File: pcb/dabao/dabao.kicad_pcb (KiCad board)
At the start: 2 copper layers, 127.8 x 107.8 mm, 68 parts, among them J1 Conn_01x05, J2 USB_C_Receptacle_USB2.0_16P, J3 Conn_01x04, J4 Conn_01x04_Pin, J5 Conn_Battery, J6 Conn_01x04, J7 Conn_01x04, J8 Display, SW1 SW_RESET, SW2 SW_POWER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

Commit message: Update layout
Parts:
- removed R4, R5: 4.7k, Resistor_SMD:R_0805_2012Metric
- J5: footprint Connector_JST:JST_EH_S2B-EH_1x02_P2.50mm_Horizontal -> Connector_JST:JST_PH_S2B-PH-K_1x02_P2.00mm_Horizontal
- JP6, R1: moved to F.Cu
- JP7: moved to B.Cu
- moved SW1 81.2 mm to (193.8, 109.8), turned to 90 degrees
- moved J6 42.7 mm to (152.8, 111.0), turned to 165 degrees
- moved J7 42.7 mm to (152.5, 112.2), turned to -15 degrees
- moved R3 28.6 mm to (209.8, 114.5), turned to -90 degrees
- moved J5 26.2 mm to (209.5, 136.5)
- moved R2 24.5 mm to (207.0, 114.5), turned to -90 degrees
- moved R1 22.9 mm to (204.2, 114.5), turned to -90 degrees
- moved JP9 17.5 mm to (202.0, 124.8), turned to -90 degrees
- moved JP10 15.1 mm to (204.8, 124.8), turned to -90 degrees
- moved JP12 12.4 mm to (211.2, 124.8), turned to -90 degrees
- moved JP11 12.4 mm to (208.5, 124.8), turned to -90 degrees
- moved JP1 12.1 mm to (214.0, 145.2)
- moved JP3 12.0 mm to (214.0, 145.2)
- moved JP2 11.9 mm to (214.0, 148.0)
- moved JP4 11.8 mm to (214.0, 148.0)
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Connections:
- J1 pad 1: /SDA_Right -> /PS2_Data
- J1 pad 3: /SCL_Right -> /PS2_CLK
- J4 pad 1: unconnected-(J4-Pin_1-Pad1) -> VDD
- J4 pad 4: unconnected-(J4-Pin_4-Pad4) -> GND
- J5 pad 1: Net-(J5-Pin_1) -> GND
- J5 pad 2: GND -> Net-(J5-Pin_2)
- SW2 pad 2: Net-(J5-Pin_1) -> Net-(J5-Pin_2)
- U1 pad 1: /SDA_Right -> unconnected-(U1-P0.06-Pad1)
- U1 pad 10: /col_index -> /SCL_Right
- U1 pad 11: /col_middle -> /SDA_Right
- U1 pad 12: /col_ring -> /row_thumb
- U1 pad 17: /MOSI -> /row_top
- U1 pad 18: /SCK -> /row_home
- U1 pad 19: /CS -> /row_bottom
- U1 pad 2: /SCL_Right -> unconnected-(U1-P0.08-Pad2)
- U1 pad 20: unconnected-(U1-P1.15-LF-Pad20) -> /col_inner
- U1 pad 21: unconnected-(U1-P1.13-LF-Pad21) -> /col_index
- U1 pad 22: unconnected-(U1-P1.11-LF-Pad22) -> /col_middle
- U1 pad 23: unconnected-(U1-P0.10-LF-Pad23) -> /col_ring
- U1 pad 5: /row_top -> /PS2_Data
- U1 pad 6: /row_home -> /PS2_CLK
- U1 pad 7: /row_bottom -> /MOSI
- U1 pad 8: /row_thumb -> /SCK
- U1 pad 9: /col_inner -> /CS
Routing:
- net /SDA_Right: track 66.4 -> 33.1 mm, vias 0 -> 2
- net /MOSI: track 0.00 -> 18.9 mm
- net /SCL_Right: track 16.8 -> 34.9 mm
- net /SCK: track 0.00 -> 16.4 mm
- net Net-(J4-Pin_3): track 6.71 -> 22.3 mm
- net Net-(J4-Pin_2): track 6.48 -> 21.5 mm
- net /CS: track 0.00 -> 13.0 mm
- net Net-(J8-Pin_1): track 0.00 -> 11.6 mm, vias 0 -> 2
- net Net-(J8-Pin_2): track 0.00 -> 11.6 mm, vias 0 -> 2
- net /SDA_Left: track 0.00 -> 7.01 mm, vias 0 -> 2
- net Net-(JP1-B): track 8.06 -> 14.4 mm
- net Net-(JP2-B): track 9.56 -> 10.2 mm, vias 1 -> 0
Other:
- board text added: "+"
- board text added: "I2C"
- board text added: "LEFT"
- board text added: "RIGHT"
- board text added: "SPI"

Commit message: Clean up schematic
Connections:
- net Net-(U1-RST) renamed /RESET
- R2 pad 2: /SCL_Left -> /SCL_Right
- R3 pad 2: /SDA_Left -> /SDA_Right
- SW2 pad 1: Net-(SW2-A) -> /BAT+
- U1 pad 1: unconnected-(U1-P0.06-Pad1) -> /PS2_Data
- U1 pad 10: /SCL_Right -> /CS
- U1 pad 11: /SDA_Right -> unconnected-(U1-P1.04-LF-Pad11)
- U1 pad 13: unconnected-(U1-BAT+-Pad13) -> /BAT+
- U1 pad 2: unconnected-(U1-P0.08-Pad2) -> /PS2_CLK
- U1 pad 29: Net-(SW2-A) -> unconnected-(U1-BAT+-Pad29)
- U1 pad 3: unconnected-(U1-GND-Pad3) -> GND
- U1 pad 4: unconnected-(U1-GND-Pad4) -> GND
- U1 pad 5: /PS2_Data -> /SDA_Right
- U1 pad 6: /PS2_CLK -> /SCL_Right
- U1 pad 7: /MOSI -> /SCK
- U1 pad 8: /SCK -> unconnected-(U1-P0.24-Pad8)
- U1 pad 9: /CS -> /MOSI
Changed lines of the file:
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@@
 	(net 43 "Net-(J3-Pin_2)")
 	(net 44 "unconnected-(U1-P1.02-LF-Pad26)")
-	(net 45 "unconnected-(U1-BAT+-Pad13)")
+	(net 45 "/RESET")
 	(net 46 "unconnected-(U1-P1.01-LF-Pad25)")
 	(net 47 "Net-(J3-Pin_3)")
-	(net 48 "unconnected-(U1-GND-Pad4)")
+	(net 48 "/BAT+")
 	(net 49 "unconnected-(U1-P1.07-LF-Pad27)")
-	(net 50 "unconnected-(U1-GND-Pad3)")
+	(net 50 "unconnected-(U1-P1.04-LF-Pad11)")
 	(net 51 "unconnected-(U2-NC-Pad14)")
 	(net 52 "Net-(J3-Pin_1)")
@@
 	(net 73 "Net-(J5-Pin_2)")
 	(net 74 "GND")
-	(net 75 "Net-(U1-RST)")
-	(net 76 "Net-(SW2-A)")
-	(net 77 "unconnected-(U1-P0.08-Pad2)")
-	(net 78 "unconnected-(U1-P0.06-Pad1)")
-	(net 79 "/PS2_Data")
-	(net 80 "/PS2_CLK")
+	(net 75 "unconnected-(U1-P0.24-Pad8)")
+	(net 76 "unconnected-(U1-BAT+-Pad29)")
+	(net 77 "/PS2_Data")
+	(net 78 "/PS2_CLK")
 	(footprint "Jumper:SolderJumper-2_P1.3mm_Open_TrianglePad1.0x1.5mm"
 		(layer "F.Cu")
@@
 			(layers "F.Cu" "F.Mask" "F.Paste")
 			(roundrect_rratio 0.243902)
-			(net 26 "/SDA_Left")
+			(net 30 "/SDA_Right")
 			(pintype "passive")
 		)
@@
 			(layers "F.Cu" "F.Mask" "F.Paste")
 			(roundrect_rratio 0.25)
-			(net 75 "Net-(U1-RST)")
+			(net 45 "/RESET")
 			(pinfunction "1")
 			(pintype "passive")
@@
 			(layers "F.Cu" "F.Mask" "F.Paste")
 			(roundrect_rratio 0.243902)
-			(net 25 "/SCL_Left")
+			(net 29 "/SCL_Right")
 			(pintype "passive")
 		)
@@
 		)
 		(fp_line
-			(start -1.5 -2.899999)
+			(start -1.5 -2.899998)
 			(end -1.5 -1.4)
 			(stroke
@@
 		(fp_line
 			(start -0.1 -2.9)
-			(end -1.5 -2.899999)
+			(end -1.5 -2.899998)
 			(stroke
 				(width 0.08)
@@
 		(fp_line
 			(start -1.5 -1.4)
-			(end -1.5 -2.899999)
+			(end -1.5 -2.899998)
 			(stroke
 				(width 0.05)
@@
 		)
 		(fp_line
-			(start -1.5 -2.899999)
+			(start -1.5 -2.899998)
 			(end 1.5 -2.9)
 			(stroke
@@
 		)
 		(fp_line
-			(start -1.5 -2.899999)
+			(start -1.5 -2.899998)
 			(end -1.5 -1.4)
 			(stroke
@@
 		(fp_line
 			(start -0.1 -2.9)
-			(end -1.5 -2.899999)
+			(end -1.5 -2.899998)
 			(stroke
 				(width 0.08)
@@
 			(layers "F.Cu" "F.Mask" "F.Paste")
 			(roundrect_rratio 0.15)
-			(net 76 "Net-(SW2-A)")
+			(net 48 "/BAT+")
 			(pinfunction "A")
 			(pintype "passive")
@@
 		)
 		(fp_line
-			(start 7 4.999999)
+			(start 7 4.999998)
 			(end 9.5 5)
 			(stroke
@@
 		)
 		(fp_line
-			(start 7 4.999999)
+			(start 7 4.999998)
 			(end 9.5 5)
 			(stroke
@@
 		)
 		(fp_line
-			(start 7 4.999999)
+			(start 7 4.999998)
 			(end 9.5 5)
 			(stroke
@@
 		)
 		(fp_line
-			(start 7 4.999999)
+			(start 7 4.999998)
 			(end 9.5 5)
 			(stroke
@@
 		)
 		(fp_line
-			(start 7 4.999999)
+			(start 7 4.999998)
 			(end 9.5 5)
 			(stroke
@@
 		)
 		(fp_line
-			(start 7 4.999999)
+			(start 7 4.999998)
 			(end 9.5 5)
 			(stroke
@@
 		)
 		(fp_line
-			(start 7 4.999999)
+			(start 7 4.999998)
 			(end 9.5 5)
 			(stroke
@@
 		)
 		(fp_line
-			(start 7 4.999999)
+			(start 7 4.999998)
 			(end 9.5 5)
 			(stroke
@@
 			(layers "*.Cu" "F.Mask")
 			(remove_unused_layers no)
-			(net 78 "unconnected-(U1-P0.06-Pad1)")
+			(net 77 "/PS2_Data")
 			(pinfunction "P0.06")
 			(pintype "bidirectional")
@@
 			(layers "*.Cu" "F.Mask")
 			(remove_unused_layers no)
-			(net 77 "unconnected-(U1-P0.08-Pad2)")
+			(net 78 "/PS2_CLK")
 			(pinfunction "P0.08")
 			(pintype "bidirectional")
@@
 			(remove_unused_layers no)
 			(roundrect_rratio 0.25)
-			(net 50 "unconnected-(U1-GND-Pad3)")
+			(net 74 "GND")
 			(pinfunction "GND")
 			(pintype "power_out")
@@
 			(remove_unused_layers no)
 			(roundrect_rratio 0.25)
-			(net 48 "unconnected-(U1-GND-Pad4)")
+			(net 74 "GND")
 			(pinfunction "GND")
 			(pintype "power_out")
@@
 			(layers "*.Cu" "F.Mask")
 			(remove_unused_layers no)
-			(net 79 "/PS2_Data")
+			(net 30 "/SDA_Right")
 			(pinfunction "P0.17")
 			(pintype "bidirectional")
@@
 			(layers "*.Cu" "F.Mask")
 			(remove_unused_layers no)
-			(net 80 "/PS2_CLK")
+			(net 29 "/SCL_Right")
 			(pinfunction "P0.20")
 			(pintype "bidirectional")
@@
 			(layers "*.Cu" "F.Mask")
 			(remove_unused_layers no)
-			(net 71 "/MOSI")
+			(net 72 "/SCK")
 			(pinfunction "P0.22")
 			(pintype "bidirectional")
@@
 			(layers "*.Cu" "F.Mask")
 			(remove_unused_layers no)
-			(net 72 "/SCK")
+			(net 75 "unconnected-(U1-P0.24-Pad8)")
 			(pinfunction "P0.24")
 			(pintype "bidirectional")
@@
 			(layers "*.Cu" "F.Mask")
 			(remove_unused_layers no)
-			(net 70 "/CS")
+			(net 71 "/MOSI")
 			(pinfunction "P1.00")
 			(pintype "bidirectional")
@@
 			(layers "*.Cu" "F.Mask")
 			(remove_unused_layers no)
-			(net 29 "/SCL_Right")
+			(net 70 "/CS")
 			(pinfunction "P0.11")
 			(pintype "bidirectional")
@@
 			(layers "*.Cu" "F.Mask")
 			(remove_unused_layers no)
-			(net 30 "/SDA_Right")
+			(net 50 "unconnected-(U1-P1.04-LF-Pad11)")
 			(pinfunction "P1.04-LF")
 			(pintype "bidirectional")
@@
 			(layers "*.Cu" "F.Mask")
 			(remove_unused_layers no)
-			(net 45 "unconnected-(U1-BAT+-Pad13)")
+			(net 48 "/BAT+")
 			(pinfunction "BAT+")
 			(pintype "power_out")
@@
 			(layers "*.Cu" "F.Mask")
 			(remove_unused_layers no)
-			(net 75 "Net-(U1-RST)")
+			(net 45 "/RESET")
 			(pinfunction "RST")
 			(pintype "bidirectional")
@@
 			(layers "*.Cu" "F.Mask")
 			(remove_unused_layers no)
-			(net 76 "Net-(SW2-A)")
+			(net 76 "unconnected-(U1-BAT+-Pad29)")
 			(pinfunction "BAT+")
 			(pintype "power_out")
@@
 		)
 		(fp_line
-			(start 7 4.999999)
+			(start 7 4.999998)
 			(end 9.5 5)
 			(stroke
@@
 		)
 		(fp_line
-			(start 7 4.999999)
+			(start 7 4.999998)
 			(end 9.5 5)
 			(stroke
@@
 			(layers "B.Cu" "B.Mask" "B.Paste")
 			(roundrect_rratio 0.25)
-			(net 79 "/PS2_Data")
+			(net 77 "/PS2_Data")
 			(pinfunction "Pin_1")
 			(pintype "passive")
@@
 			(layers "B.Cu" "B.Mask" "B.Paste")
 			(roundrect_rratio 0.25)
-			(net 80 "/PS2_CLK")
+			(net 78 "/PS2_CLK")
 			(pinfunction "Pin_3")
 			(pintype "passive")
@@
 		)
 		(fp_line
-			(start 7 4.999999)
+			(start 7 4.999998)
 			(end 9.5 5)
 			(stroke
@@
 		)
 		(fp_line
-			(start 7 4.999999)
+			(start 7 4.999998)
 			(end 9.5 5)
 			(stroke
@@
 		)
 		(fp_line
-			(start 7 4.999999)
+			(start 7 4.999998)
 			(end 9.5 5)
 			(stroke
@@
 		)
 		(fp_line
-			(start 7 4.999999)
+			(start 7 4.999998)
 			(end 9.5 5)
 			(stroke

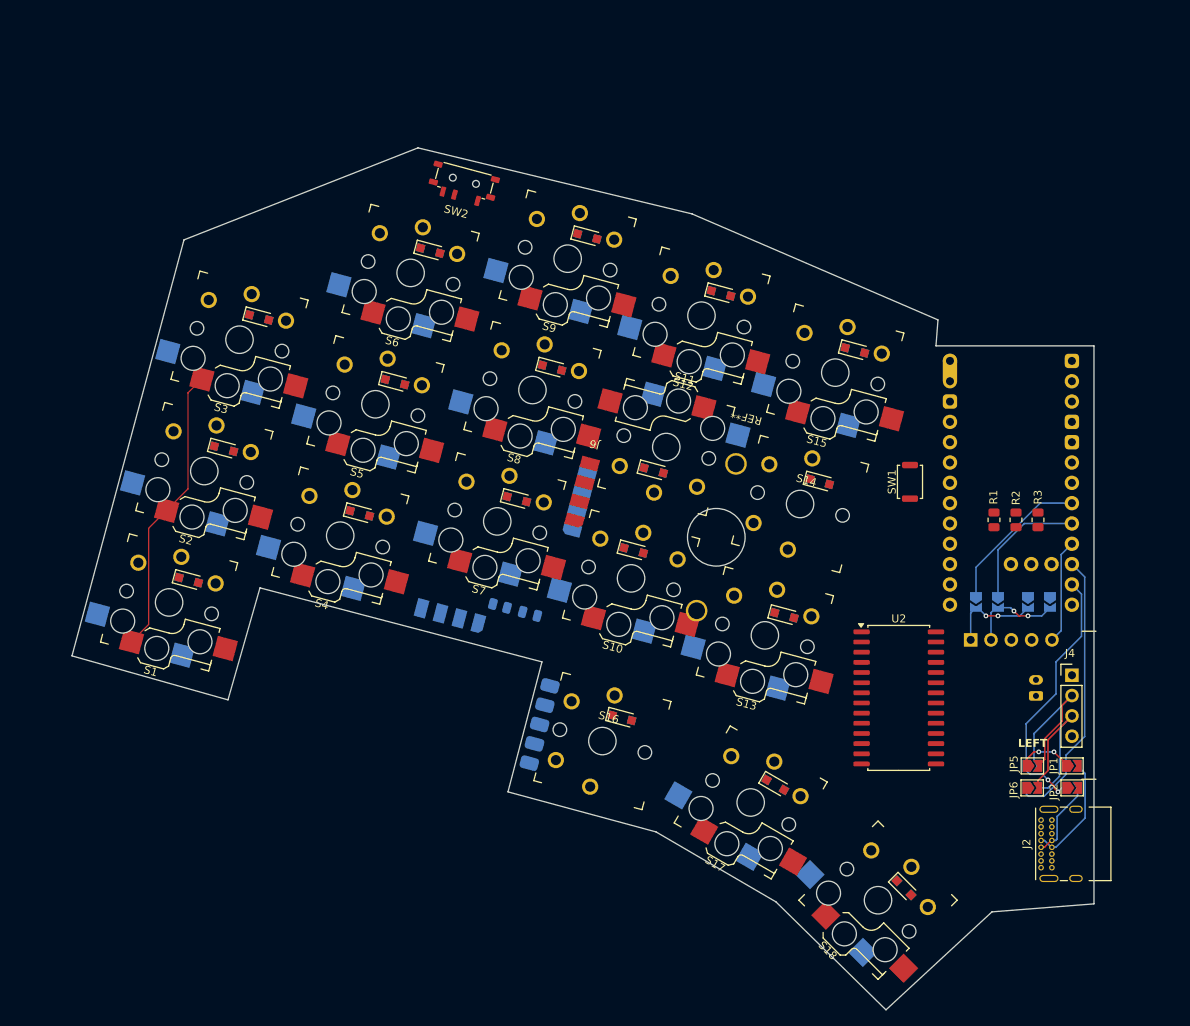
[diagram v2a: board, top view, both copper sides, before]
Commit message: Fix connectors in layout, add board outline, start routing
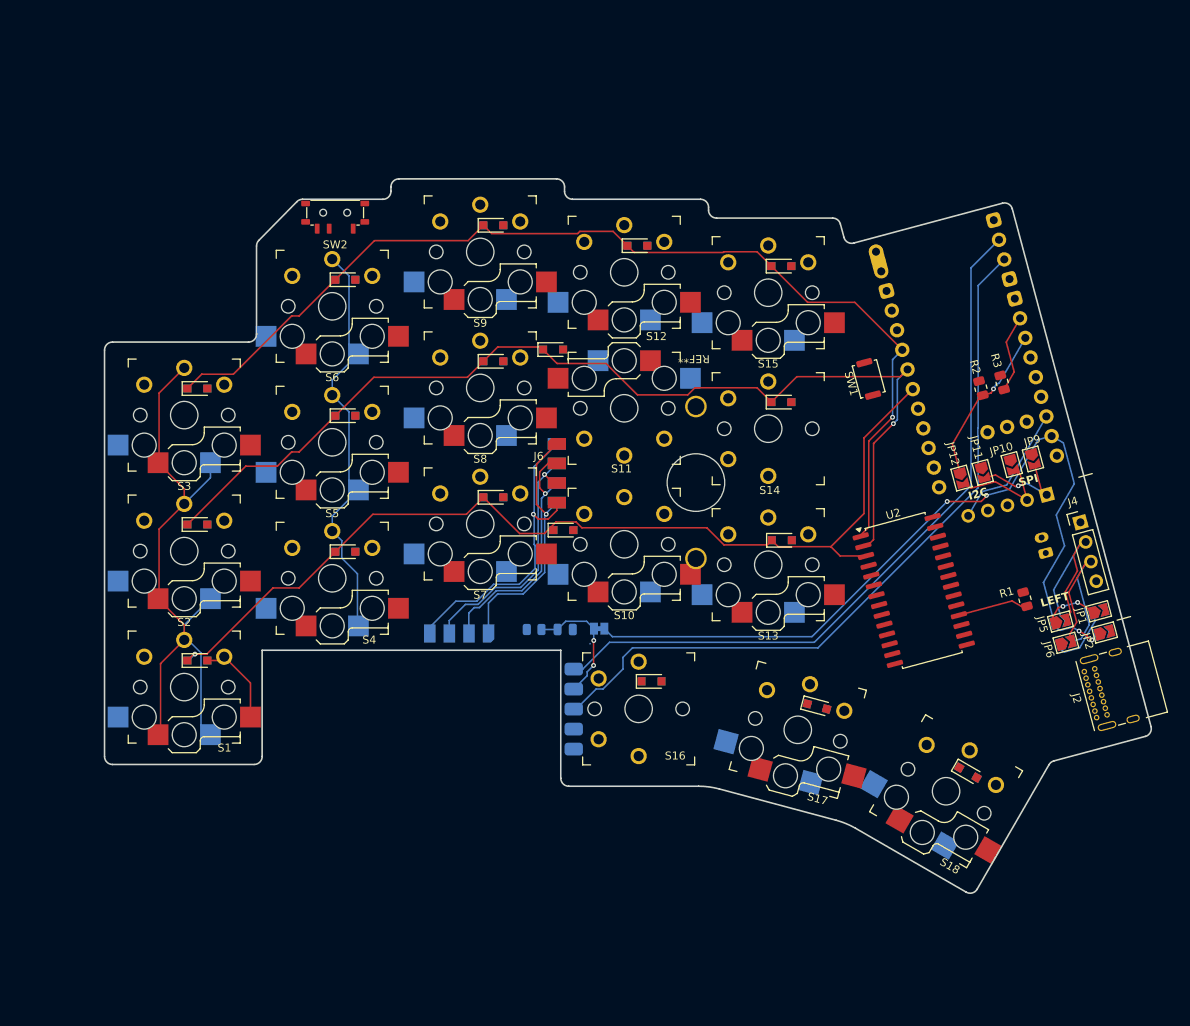
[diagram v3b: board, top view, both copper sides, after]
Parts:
- added JP13: SolderJumper_2_Bridged, Jumper:SolderJumper-2_P1.3mm_Bridged_Pad1.0x1.5mm, B.Cu at (154.9, 128.1)
- J4: value Conn_01x04_Pin -> MagConn_01x04_Pin
- JP10, JP11, JP12, JP9: moved to F.Cu
- moved J8 20.5 mm to (210.8, 111.4), turned to 105 degrees
- moved J2 20.0 mm to (217.1, 139.2), turned to 105 degrees
- moved JP2 19.8 mm to (218.1, 128.6), turned to 15 degrees
- moved JP4 19.8 mm to (218.0, 128.6), turned to 15 degrees
- moved D11 19.7 mm to (149.1, 93.2), turned to 0 degrees
- moved JP1 19.6 mm to (217.3, 125.9), turned to 15 degrees
- moved JP3 19.6 mm to (217.3, 125.9), turned to 15 degrees
- moved JP9 19.2 mm to (209.1, 106.9), turned to -75 degrees
- moved J4 19.1 mm to (215.1, 114.8), turned to 15 degrees
- moved JP12 19.0 mm to (200.2, 109.3), turned to -75 degrees
- moved JP6 18.6 mm to (213.2, 129.9), turned to 15 degrees
- moved JP8 18.6 mm to (213.2, 129.9), turned to 15 degrees
- moved JP5 18.4 mm to (212.6, 127.2), turned to 15 degrees
- moved JP7 18.4 mm to (212.5, 127.2), turned to 15 degrees
- moved J5 17.9 mm to (210.7, 118.6), turned to 105 degrees
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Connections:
- U1 pad 11: unconnected-(U1-P1.04-LF-Pad11) -> /TP_reset
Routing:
- net /row_top: track 0.00 -> 130.0 mm, vias 0 -> 1
- net /row_home: track 0.00 -> 129.1 mm, vias 0 -> 1
- net /row_bottom: track 0.00 -> 123.2 mm, vias 0 -> 1
- net /PS2_CLK: track 0.00 -> 92.8 mm
- net /PS2_Data: track 0.00 -> 91.3 mm
- net /TP_reset: track 0.00 -> 67.1 mm, vias 0 -> 2
- net /col_ring: track 0.00 -> 52.6 mm
- net /col_pinky: track 36.5 -> 79.1 mm
- net Net-(J3-Pin_4): track 0.00 -> 38.4 mm, vias 0 -> 1
- net Net-(J3-Pin_1): track 0.00 -> 31.4 mm, vias 0 -> 1
- net Net-(J3-Pin_3): track 0.00 -> 30.9 mm, vias 0 -> 1
- net Net-(J3-Pin_2): track 0.00 -> 30.5 mm, vias 0 -> 1
- net /MOSI: track 18.9 -> 0.00 mm
- net /SCK: track 16.4 -> 0.00 mm
- net Net-(J1-Pin_2): track 0.00 -> 16.1 mm, vias 0 -> 2
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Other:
- board size 127.8 x 107.8 mm -> 130.8 x 89.3 mm

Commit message: Add missing pullups on ps2 lines
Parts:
- added R4: 4.7k, Resistor_SMD:R_0805_2012Metric, F.Cu at (197.5, 99.4)
- added R5: 4.7k, Resistor_SMD:R_0805_2012Metric, F.Cu at (200.0, 98.8)
